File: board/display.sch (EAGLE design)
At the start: 39 parts, among them IC1 MEGA8-P, IC2 74HCT595N, IC3 7805T, Q1 8MHz, Q2 MMBT4403LT1SMD, Q3 MMBT4403LT1SMD, Q4 MMBT4403LT1SMD, Q5 MMBT4403LT1SMD, X1 MKDSN1,5/2-5,08

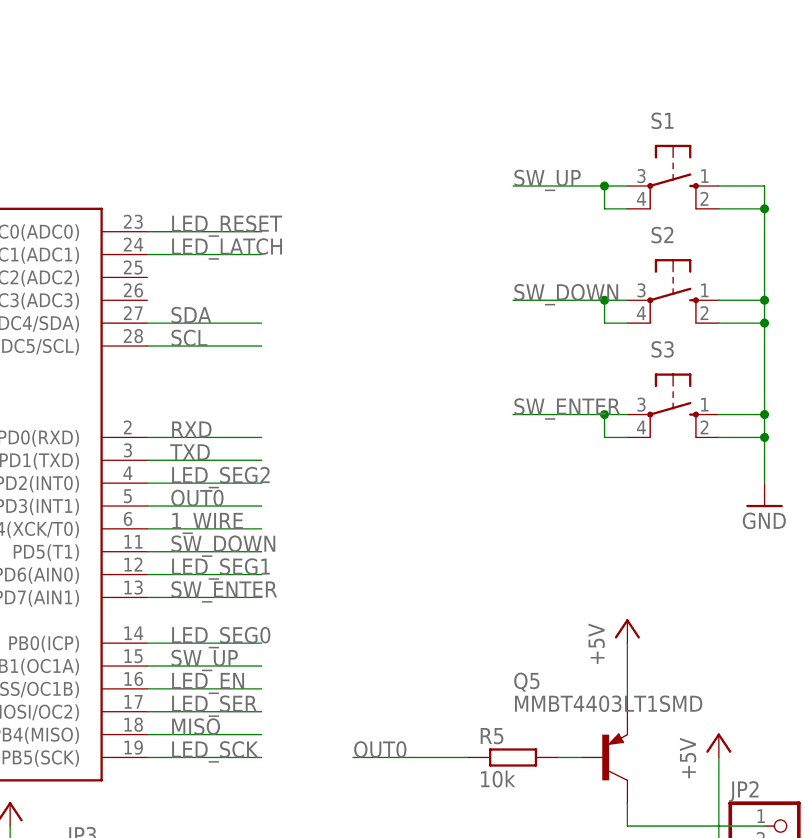
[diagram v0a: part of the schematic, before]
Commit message: working buttons and set temperature
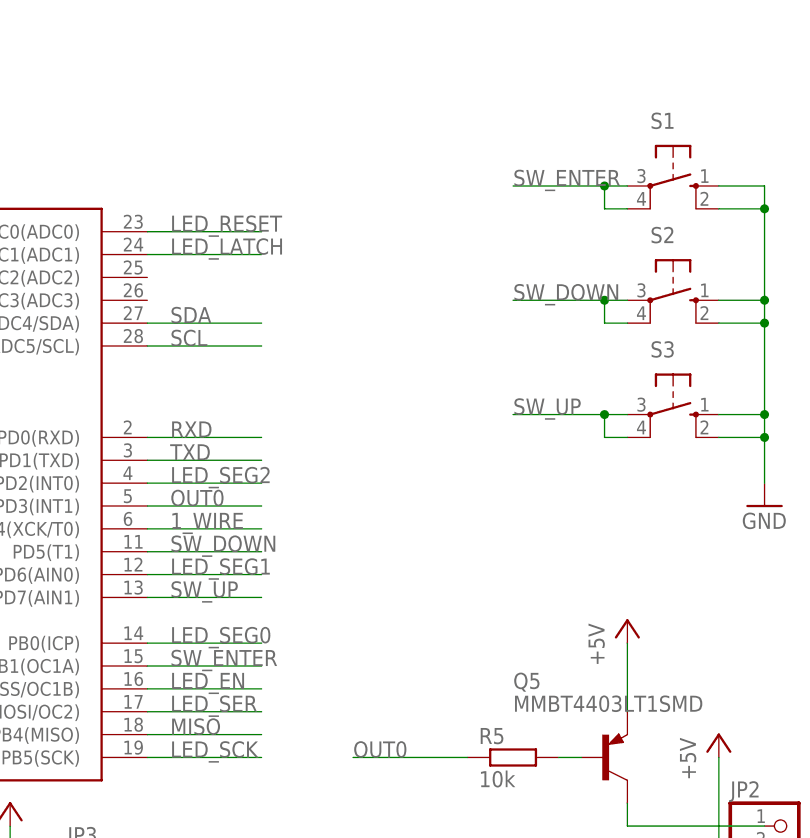
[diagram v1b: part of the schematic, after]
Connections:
- net SW_ENTER: now also IC1.PB1(OC1A), S1.P, S1.P1; no longer IC1.PD7(AIN1), S3.P, S3.P1
- net SW_UP: now also IC1.PD7(AIN1), S3.P, S3.P1; no longer IC1.PB1(OC1A), S1.P, S1.P1
